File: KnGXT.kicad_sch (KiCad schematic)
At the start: 112 parts, among them J1 USB_C_ReceptacleUSB2.0, J2 Conn_01x10_Male, SW1 RotaryEncoder_Switch, SW10 SW_Push, SW11 SW_Push, SW12 SW_Push, SW13 SW_Push, SW14 SW_Push, SW15 SW_Push, SW16 SW_Push, SW17 SW_Push, SW2 RotaryEncoder_Switch, SW3 SW_Push, SW4 SW_Push, SW5 SW_Push, SW6 SW_Push, SW7 SW_Push, SW8 SW_Push, SW9 SW_Push, U1 AMS1117-3.3, U2 W25Q128JVS, U3 RP2040, U4 74125, Y1 12MHz

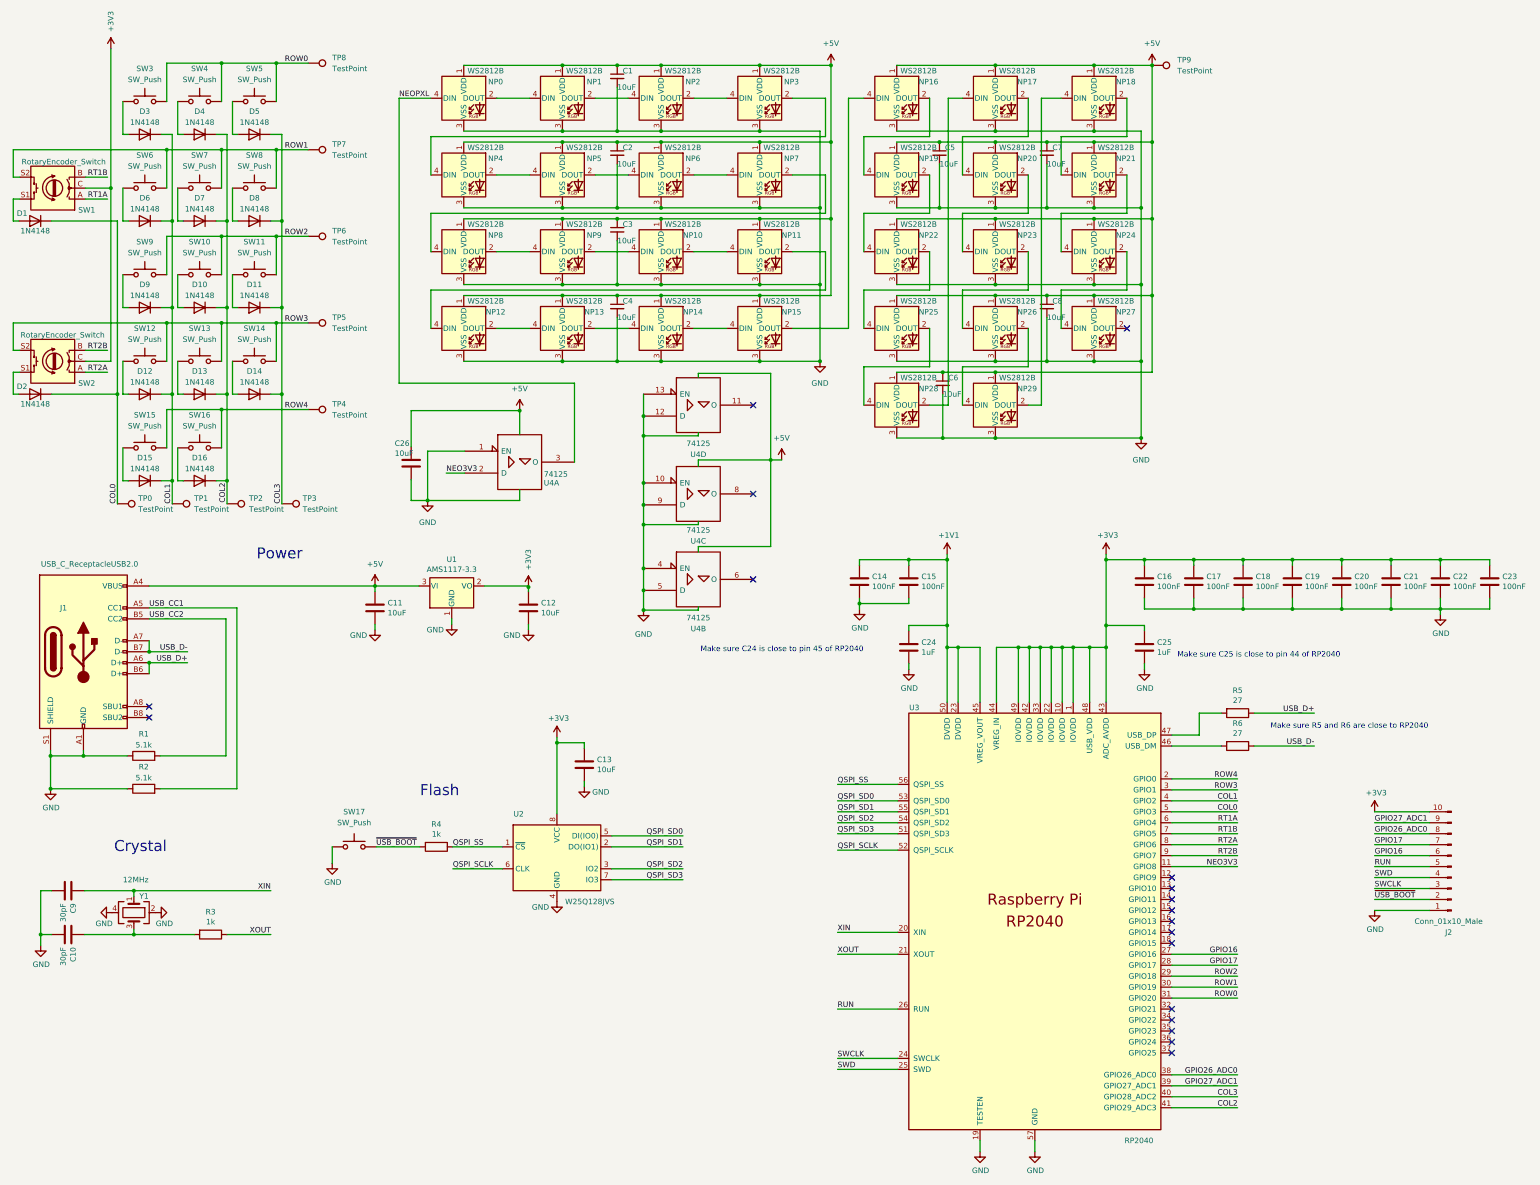
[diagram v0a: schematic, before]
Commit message: Update the world to switch to 3.5x2.8mm WS2812B LEDs
Signed-off-by: Flynn <flynn+github@kodachi.com>
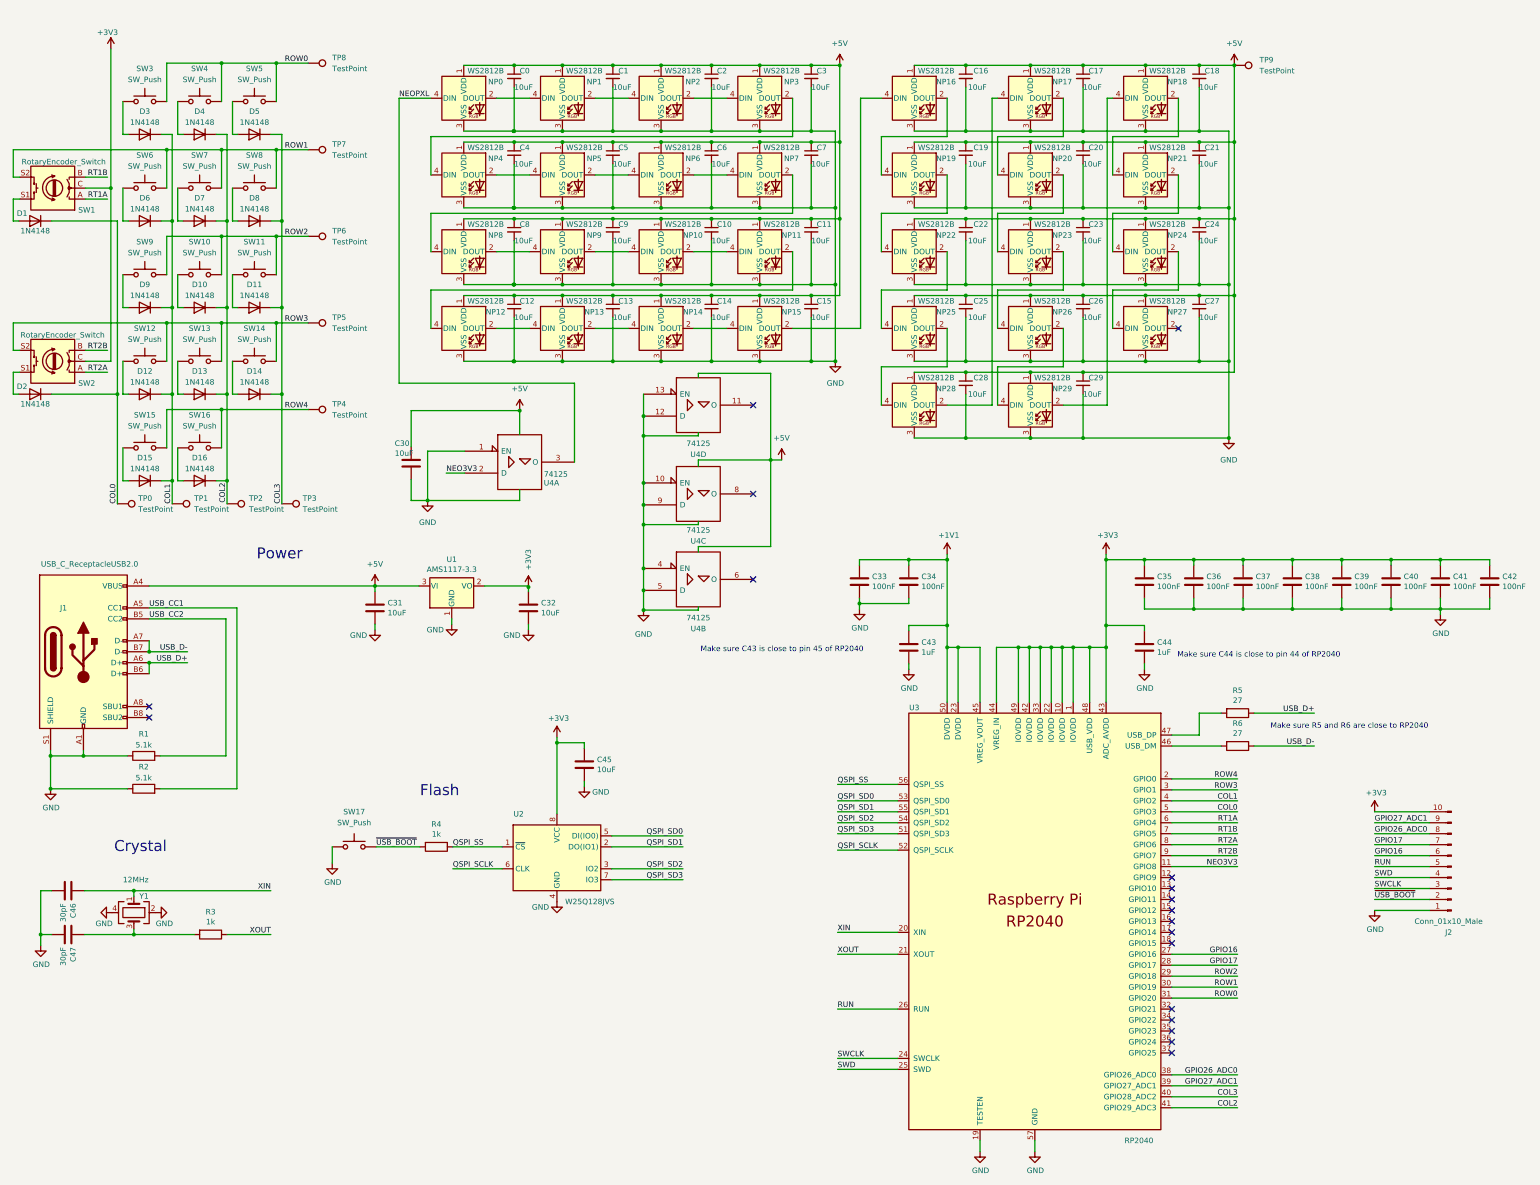
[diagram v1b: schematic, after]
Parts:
- added C0, C10, C11, C12, C14, C15, C16, C17, C18, C2, C21, C22, C23, C24, C25, C27, C29, C3, C4, C6, C7, C8: 10uF, Capacitor_SMD:C_0402_1005Metric, symbol Device:C_Small
- U3: footprint RP2040_minimal:RP2040-QFN-56 -> RP_Silicon:RP2040-QFN-56; symbol MCU_RaspberryPi_RP2040:RP2040 -> RP_Silicon:RP2040
- renumbered C4 to C13, C5 to C19, C7 to C20, C8 to C26, C6 to C28, C26 to C30, C11 to C31, C12 to C32, C14 to C33, C15 to C34, C16 to C35, C17 to C36, C18 to C37, C19 to C38, C20 to C39, C21 to C40, C22 to C41, C23 to C42, C24 to C43, C25 to C44, C13 to C45, C9 to C46, C10 to C47, C2 to C5, C3 to C9
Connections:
- net +5V: now also C0.1, C10.1, C11.1, C12.1, C14.1, C15.1, C16.1, C17.1, C18.1, C2.1, C21.1, C22.1, C23.1, C24.1, C25.1, C27.1, C29.1, C3.1, C4.1, C6.1, C7.1, C8.1
- net GND: now also C0.2, C10.2, C11.2, C12.2, C14.2, C15.2, C16.2, C17.2, C18.2, C2.2, C21.2, C22.2, C23.2, C24.2, C25.2, C27.2, C29.2, C3.2, C4.2, C6.2, C7.2, C8.2
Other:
- note added: "Make sure C43 is close to pin 45 of RP2040"
- note added: "Make sure C44 is close to pin 44 of RP2040"
- note removed: "Make sure C24 is close to pin 45 of RP2040"
- note removed: "Make sure C25 is close to pin 44 of RP2040"
- moved on the sheet: C1, C13, C19, C20, C26, C28, C5, C9, NP16, NP17, NP18, NP19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

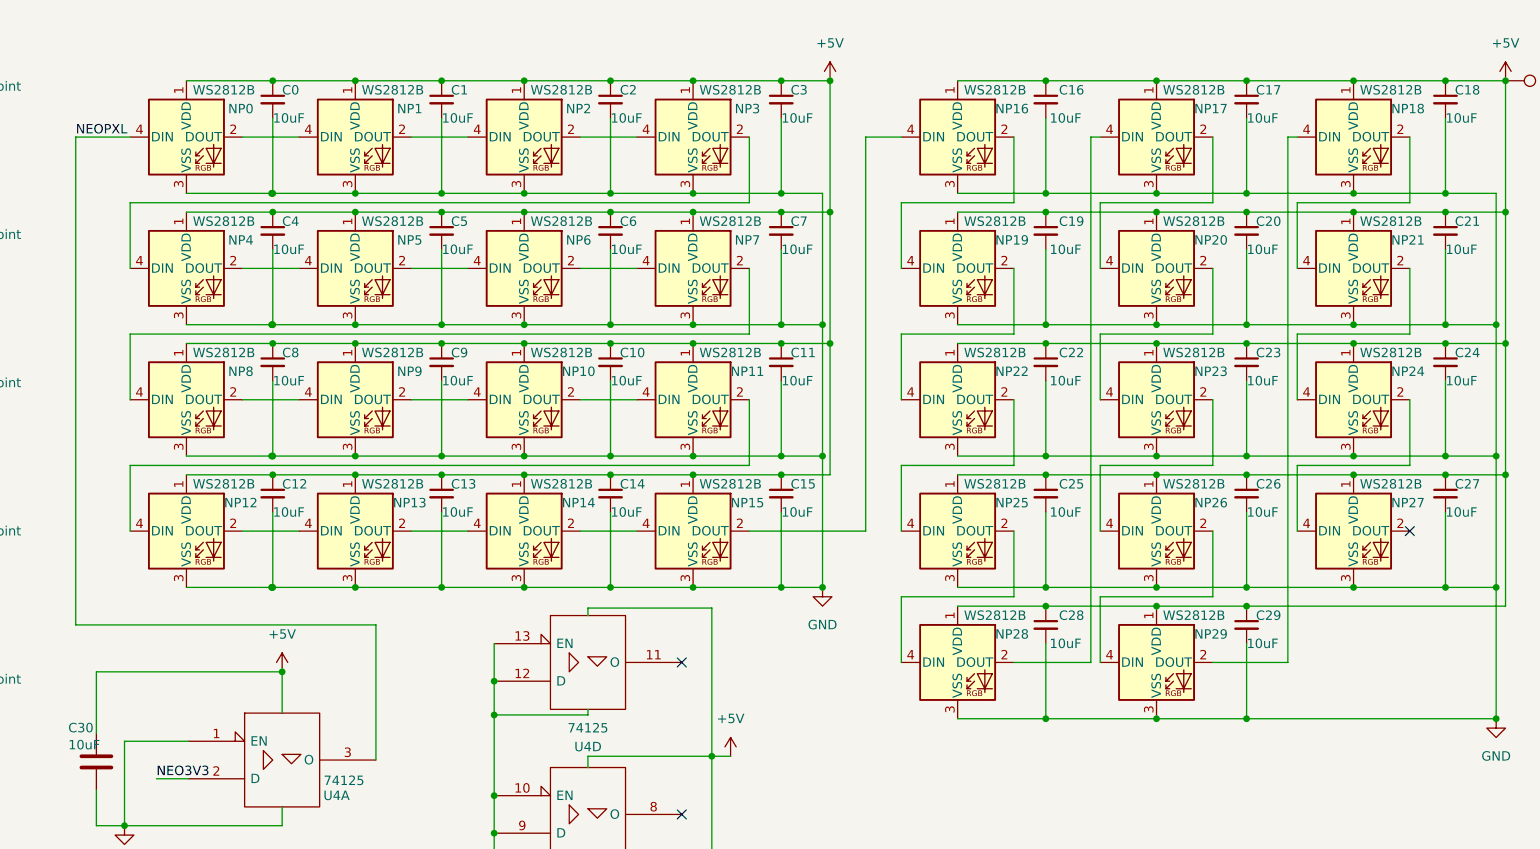
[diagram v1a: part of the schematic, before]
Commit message: Swap the WS2812B _AGAIN_ since the C965557 is out of stock
Thankfully the C2890364 is identical to the C965557, just
rotated 180 degrees.

Signed-off-by: Flynn <flynn+github@kodachi.com>
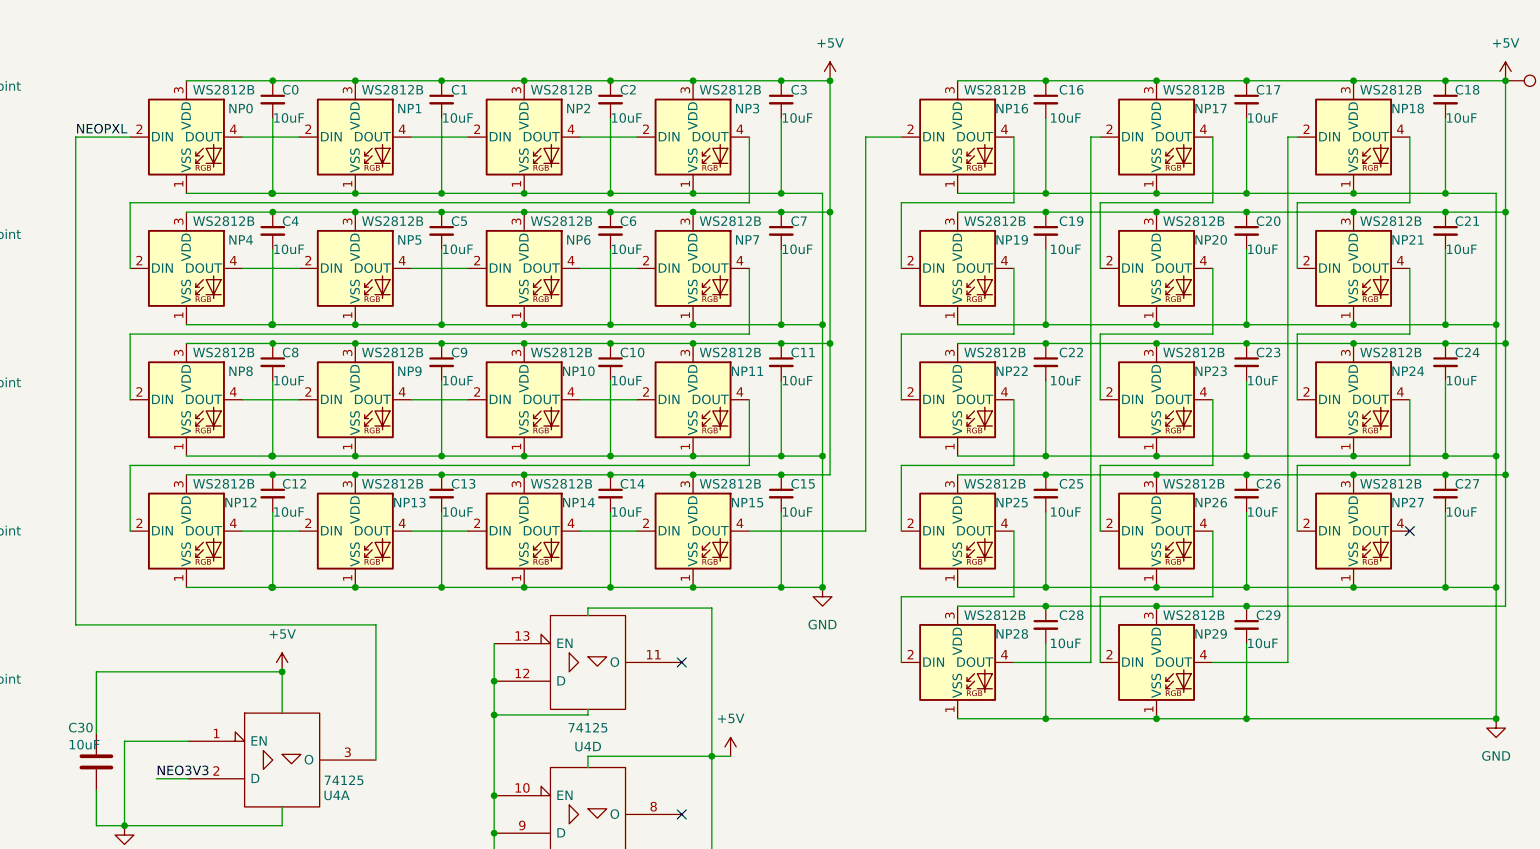
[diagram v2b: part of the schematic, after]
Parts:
- NP0, NP1, NP10, NP11, NP12, NP13, NP14, NP15, NP16, NP17, NP18, NP19, NP2, NP20, NP21, NP22, NP23, NP24, NP25, NP26, NP27, NP28, NP29, NP3, NP4, NP5, NP6, NP7, NP8, NP9: footprint LED_SMD:LED_WS2812B_PLCC4_3.5x2.8mm_P1.5mm -> LED_SMD:LED_WS2812B_3.5x2.8_C2890364; symbol LED:WS2812B -> LED:WS2812B_C2890364; LCSC C965557 -> C2890364
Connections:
- net +5V: now also NP0.3 (VDD), NP1.3 (VDD), NP10.3 (VDD), NP11.3 (VDD), NP12.3 (VDD), NP13.3 (VDD), NP14.3 (VDD), NP15.3 (VDD), NP16.3 (VDD), NP17.3 (VDD), NP18.3 (VDD), NP19.3 (VDD), NP2.3 (VDD), NP20.3 (VDD), NP21.3 (VDD), NP22.3 (VDD), NP23.3 (VDD), NP24.3 (VDD), NP25.3 (VDD), NP26.3 (VDD), NP27.3 (VDD), NP28.3 (VDD), NP29.3 (VDD), NP3.3 (VDD), NP4.3 (VDD), NP5.3 (VDD), NP6.3 (VDD), NP7.3 (VDD), NP8.3 (VDD), NP9.3 (VDD); no longer NP0.1 (VDD), NP1.1 (VDD), NP10.1 (VDD), NP11.1 (VDD), NP12.1 (VDD), NP13.1 (VDD), NP14.1 (VDD), NP15.1 (VDD), NP16.1 (VDD), NP17.1 (VDD), NP18.1 (VDD), NP19.1 (VDD), NP2.1 (VDD), NP20.1 (VDD), NP21.1 (VDD), NP22.1 (VDD), NP23.1 (VDD), NP24.1 (VDD), NP25.1 (VDD), NP26.1 (VDD), NP27.1 (VDD), NP28.1 (VDD), NP29.1 (VDD), NP3.1 (VDD), NP4.1 (VDD), NP5.1 (VDD), NP6.1 (VDD), NP7.1 (VDD), NP8.1 (VDD), NP9.1 (VDD)
- net GND: now also NP0.1 (VSS), NP1.1 (VSS), NP10.1 (VSS), NP11.1 (VSS), NP12.1 (VSS), NP13.1 (VSS), NP14.1 (VSS), NP15.1 (VSS), NP16.1 (VSS), NP17.1 (VSS), NP18.1 (VSS), NP19.1 (VSS), NP2.1 (VSS), NP20.1 (VSS), NP21.1 (VSS), NP22.1 (VSS), NP23.1 (VSS), NP24.1 (VSS), NP25.1 (VSS), NP26.1 (VSS), NP27.1 (VSS), NP28.1 (VSS), NP29.1 (VSS), NP3.1 (VSS), NP4.1 (VSS), NP5.1 (VSS), NP6.1 (VSS), NP7.1 (VSS), NP8.1 (VSS), NP9.1 (VSS); no longer NP0.3 (VSS), NP1.3 (VSS), NP10.3 (VSS), NP11.3 (VSS), NP12.3 (VSS), NP13.3 (VSS), NP14.3 (VSS), NP15.3 (VSS), NP16.3 (VSS), NP17.3 (VSS), NP18.3 (VSS), NP19.3 (VSS), NP2.3 (VSS), NP20.3 (VSS), NP21.3 (VSS), NP22.3 (VSS), NP23.3 (VSS), NP24.3 (VSS), NP25.3 (VSS), NP26.3 (VSS), NP27.3 (VSS), NP28.3 (VSS), NP29.3 (VSS), NP3.3 (VSS), NP4.3 (VSS), NP5.3 (VSS), NP6.3 (VSS), NP7.3 (VSS), NP8.3 (VSS), NP9.3 (VSS)
- net NEOPXL: now also NP0.2 (DIN); no longer NP0.4 (DIN)
- net at NP8.2 (DIN): now also NP7.4 (DOUT); no longer NP9.4 (DIN)
- net at NP8.4 (DOUT): now also NP9.2 (DIN); no longer NP7.2 (DOUT)
- net at NP25.2 (DIN): now also NP22.4 (DOUT); no longer NP28.4 (DIN)
- net at NP25.4 (DOUT): now also NP28.2 (DIN); no longer NP22.2 (DOUT)
- net at NP27.2 (DIN): now also NP24.4 (DOUT)
- net at NP27.4 (DOUT): no longer NP24.2 (DOUT)
- net at NP13.2 (DIN): now also NP12.4 (DOUT); no longer NP14.4 (DIN)
- net at NP13.4 (DOUT): now also NP14.2 (DIN); no longer NP12.2 (DOUT)
- net at NP19.2 (DIN): now also NP16.4 (DOUT); no longer NP22.4 (DIN)
- net at NP18.2 (DIN): now also NP29.4 (DOUT); no longer NP21.4 (DIN)
- net at NP18.4 (DOUT): now also NP21.2 (DIN); no longer NP29.2 (DOUT)
- net at NP20.2 (DIN): now also NP17.4 (DOUT); no longer NP23.4 (DIN)
- net at NP20.4 (DOUT): now also NP23.2 (DIN); no longer NP17.2 (DOUT)
- net at NP1.2 (DIN): now also NP0.4 (DOUT); no longer NP2.4 (DIN)
- net at NP1.4 (DOUT): now also NP2.2 (DIN); no longer NP0.2 (DOUT)
- net at NP3.2 (DIN): now also NP2.4 (DOUT); no longer NP4.4 (DIN)
- net at NP3.4 (DOUT): now also NP4.2 (DIN); no longer NP2.2 (DOUT)
- net at NP19.4 (DOUT): now also NP22.2 (DIN); no longer NP16.2 (DOUT)
- net at NP10.2 (DIN): now also NP9.4 (DOUT); no longer NP11.4 (DIN)
- net at NP10.4 (DOUT): now also NP11.2 (DIN); no longer NP9.2 (DOUT)
- net at NP26.2 (DIN): now also NP23.4 (DOUT); no longer NP29.4 (DIN)
- net at NP26.4 (DOUT): now also NP29.2 (DIN); no longer NP23.2 (DOUT)
- net at NP6.2 (DIN): now also NP5.4 (DOUT); no longer NP7.4 (DIN)
- net at NP15.2 (DIN): now also NP14.4 (DOUT); no longer NP16.4 (DIN)
- net at NP15.4 (DOUT): now also NP16.2 (DIN); no longer NP14.2 (DOUT)
- net at NP6.4 (DOUT): now also NP7.2 (DIN); no longer NP5.2 (DOUT)
- new net: NP17.2 (DIN), NP28.4 (DOUT)
- new net: NP21.4 (DOUT), NP24.2 (DIN)
- new net: NP4.4 (DOUT), NP5.2 (DIN)
- new net: NP11.4 (DOUT), NP12.2 (DIN)
